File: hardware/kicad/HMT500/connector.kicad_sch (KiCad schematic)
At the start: 10 parts, among them J1 SM08B-GHS-TB, J5 Chassis contact

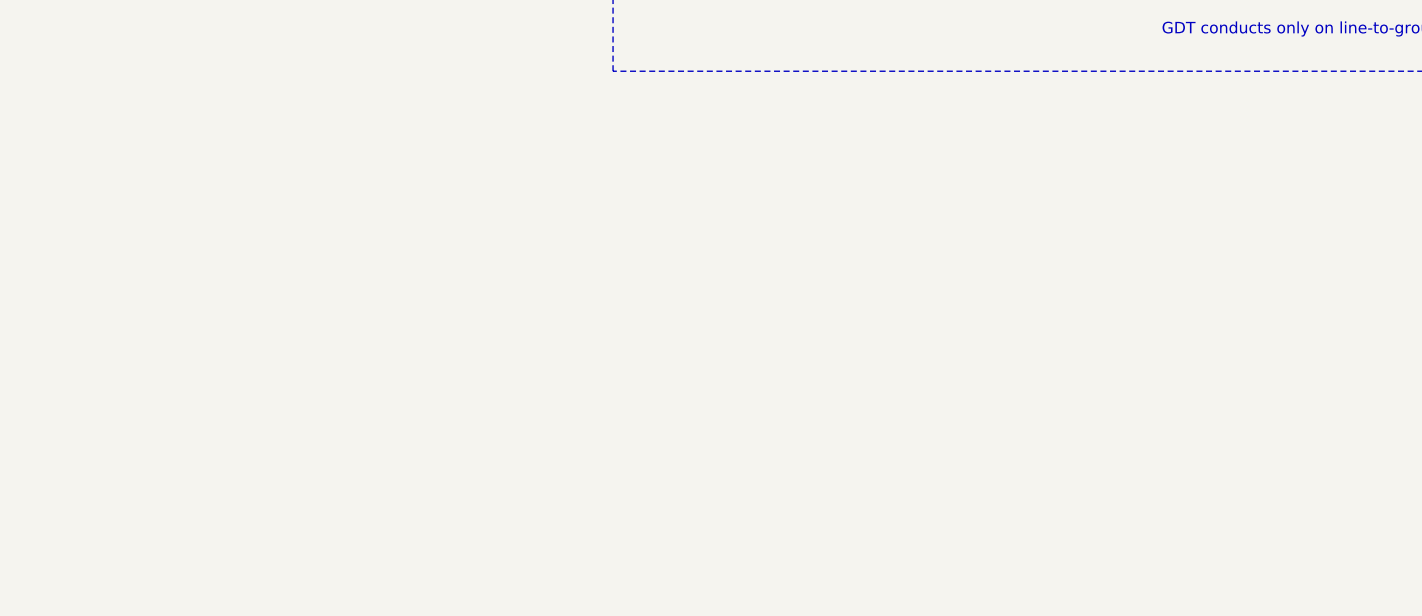
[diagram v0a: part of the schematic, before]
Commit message: Schematic: key-parts table (role, features, specs) on every sheet
- Aligned 4-column table per sheet: reference, part, role, features/specs;
  values still to confirm against datasheets marked with *
- Connector and RS-485 sheets moved to A3 for room
- New checks: text and boxes stay inside the page and out of the title block;
  every character of Hangul text must exist in NanumGothic (minus sign and micro
  sign substituted)

Co-Authored-By: Claude Opus 5.5 <noreply@anthropic.com>
Claude-Session: https://claude.ai/code/session_01JA2o8uJsqp9Vzsg4b665ev
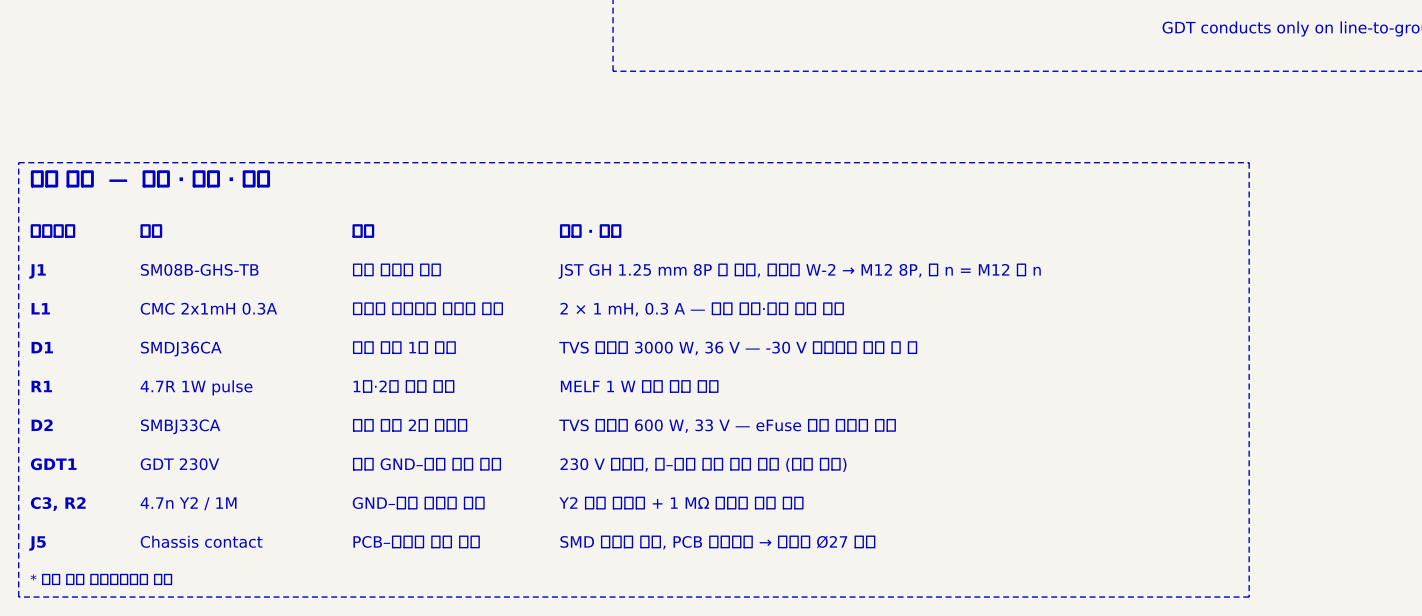
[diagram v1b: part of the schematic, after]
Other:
- note added: "* 표시 값은 데이터시트로 확인"
- note added: "1단·2단 서지 분담"
- note added: "2 × 1 mH, 0.3 A — 전도 방출·전도 내성 대책"
- note added: "230 V 방전관, 선–대지 서지 때만 도통 (평소 절연)"
- note added: "4.7R 1W pulse"
- note added: "4.7n Y2 / 1M"
- note added: "C3, R2"
- note added: "CMC 2x1mH 0.3A"
- note added: "Chassis contact"
- note added: "D1"
- note added: "D2"
- note added: "GDT 230V"
- note added: "GDT1"
- note added: "GND–외함 고주파 결합"
- note added: "J1"
- note added: "J5"
- note added: "JST GH 1.25 mm 8P 옆 삽입, 하네스 W-2 → M12 8P, 핀 n = M12 핀 n"
- note added: "L1"
- note added: "MELF 1 W 펄스 내량 저항"
- note added: "PCB–하우징 접지 접점"
- note added: "R1"
- note added: "SM08B-GHS-TB"
- note added: "SMBJ33CA"
- note added: "SMD 스프링 접점, PCB 가장자리 → 하우징 Ø27 내면"
- note added: "SMDJ36CA"
- note added: "TVS 양방향 3000 W, 36 V — -30 V 오결선에 도통 안 함"
- note added: "TVS 양방향 600 W, 33 V — eFuse 정격 이하로 제한"
- note added: "Y2 안전 콘덴서 + 1 MΩ 정전기 방전 경로"
- note added: "부품"
- note added: "부품번호"
- note added: "역할"
- note added: "입력 서지 1단 흡수"
- note added: "입력 서지 2단 클램프"
- note added: "전원선 공통모드 노이즈 차단"
- note added: "주요 부품 — 역할 · 특징 · 사양"
- note added: "특징 · 사양"
- note added: "현장 커넥터 연결"
- note added: "회로 GND–외함 서지 방전"
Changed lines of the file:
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@@
-(kicad_sch (version 20230121) (generator eeschema) (paper "A4")
+(kicad_sch (version 20230121) (generator eeschema) (paper "A3")
 (title_block (title "HMT500  Connector & input protection") (date "2026-09-29") (rev "0.6") (company "DOTECH Co., Ltd.") (comment 1 "Oil moisture transmitter HMT500 - RS-485 + 2x V/I analog output") (comment 2 "Design notes: docs/hw/circuit-design.md") (comment 3 "VERIFY=YES parts: pin numbers LMR36006/PCAP04/DAC8760/TPS26611; TPS2660 R22"))
 (symbol (lib_id "HMT500:CONN_GH8") (at 45.72 78.74 0) (unit 1) (in_bom yes) (on_board yes) (dnp no) (property "Reference" "J1" (at 38.1 64.77 0) (effects (font (size 1.27 1.27) bold) (justify left))) (property "Value" "SM08B-GHS-TB" (at 38.1 67.056 0) (effects (font (size 1.27 1.27)) (justify left))) (property "Footprint" "Connector_JST:JST_GH_SM08B-GHS-TB_1x08-1MP_P1.25mm_Horizontal" (at 45.72 78.74 0) (effects (font (size 1.27 1.27)) hide)) (property "Datasheet" "~" (at 45.72 78.74 0) (effects (font (size 1.27 1.27)) hide)) (pin "8") (pin "6") (pin "4") (pin "5") (pin "3") (pin "2") (pin "1") (pin "7") (instances (project "HMT500" (path "/1ebb025b-11bd-5f7c-aaab-41e2a750e8b3/d8924d4b-0329-5e79-8dd6-1c12c7722a4b" (reference "J1") (unit 1)))))
@@
 (rectangle (start 78.74 48.26) (end 195.58 93.98) (stroke (width 0.1524) (type dash) (color 72 72 160 1)) (fill (type none)))
 (rectangle (start 86.36 105.41) (end 195.58 142.24) (stroke (width 0.1524) (type dash) (color 72 72 160 1)) (fill (type none)))
+(rectangle (start 20.32 152.4) (end 157.041 200.66) (stroke (width 0.1524) (type dash) (color 72 72 160 1)) (fill (type none)))
 (text "FIELD CONNECTOR" (at 26.67 51.308 0) (effects (font (size 1.6 1.6) bold) (justify left bottom)))
 (text "현장 커넥터" (at 57.696 51.308 0) (effects (font (face "NanumGothic") (size 1.4 1.4)) (justify left bottom)))
@@
 (text "GDT conducts only on line-to-ground surge" (at 147.32 138.43 0) (effects (font (size 1.27 1.27)) (justify left bottom)))
 (text "PCB-housing creepage >= 2 mm" (at 147.32 132.08 0) (effects (font (size 1.27 1.27)) (justify left bottom)))
+(text "부품번호" (at 21.59 161.036 0) (effects (font (face "NanumGothic") (size 1.27 1.27) bold) (justify left bottom)))
+(text "부품" (at 33.7871 161.036 0) (effects (font (face "NanumGothic") (size 1.27 1.27) bold) (justify left bottom)))
+(text "역할" (at 57.3456 161.036 0) (effects (font (face "NanumGothic") (size 1.27 1.27) bold) (justify left bottom)))
+(text "특징 · 사양" (at 80.3961 161.036 0) (effects (font (face "NanumGothic") (size 1.27 1.27) bold) (justify left bottom)))
+(text "J1" (at 21.59 165.354 0) (effects (font (size 1.27 1.27) bold) (justify left bottom)))
+(text "SM08B-GHS-TB" (at 33.7871 165.354 0) (effects (font (size 1.27 1.27)) (justify left bottom)))
+(text "현장 커넥터 연결" (at 57.3456 165.354 0) (effects (font (face "NanumGothic") (size 1.27 1.27)) (justify left bottom)))
+(text "JST GH 1.25 mm 8P 옆 삽입, 하네스 W-2 → M12 8P, 핀 n = M12 핀 n" (at 80.3961 165.354 0) (effects (font (face "NanumGothic") (size 1.27 1.27)) (justify left bottom)))
+(text "L1" (at 21.59 169.672 0) (effects (font (size 1.27 1.27) bold) (justify left bottom)))
+(text "CMC 2x1mH 0.3A" (at 33.7871 169.672 0) (effects (font (size 1.27 1.27)) (justify left bottom)))
+(text "전원선 공통모드 노이즈 차단" (at 57.3456 169.672 0) (effects (font (face "NanumGothic") (size 1.27 1.27)) (justify left bottom)))
+(text "2 × 1 mH, 0.3 A — 전도 방출·전도 내성 대책" (at 80.3961 169.672 0) (effects (font (face "NanumGothic") (size 1.27 1.27)) (justify left bottom)))
+(text "D1" (at 21.59 173.99 0) (effects (font (size 1.27 1.27) bold) (justify left bottom)))
+(text "SMDJ36CA" (at 33.7871 173.99 0) (effects (font (size 1.27 1.27)) (justify left bottom)))
+(text "입력 서지 1단 흡수" (at 57.3456 173.99 0) (effects (font (face "NanumGothic") (size 1.27 1.27)) (justify left bottom)))
+(text "TVS 양방향 3000 W, 36 V — -30 V 오결선에 도통 안 함" (at 80.3961 173.99 0) (effects (font (face "NanumGothic") (size 1.27 1.27)) (justify left bottom)))
+(text "R1" (at 21.59 178.308 0) (effects (font (size 1.27 1.27) bold) (justify left bottom)))
+(text "4.7R 1W pulse" (at 33.7871 178.308 0) (effects (font (size 1.27 1.27)) (justify left bottom)))
+(text "1단·2단 서지 분담" (at 57.3456 178.308 0) (effects (font (face "NanumGothic") (size 1.27 1.27)) (justify left bottom)))
+(text "MELF 1 W 펄스 내량 저항" (at 80.3961 178.308 0) (effects (font (face "NanumGothic") (size 1.27 1.27)) (justify left bottom)))
+(text "D2" (at 21.59 182.626 0) (effects (font (size 1.27 1.27) bold) (justify left bottom)))
+(text "SMBJ33CA" (at 33.7871 182.626 0) (effects (font (size 1.27 1.27)) (justify left bottom)))
+(text "입력 서지 2단 클램프" (at 57.3456 182.626 0) (effects (font (face "NanumGothic") (size 1.27 1.27)) (justify left bottom)))
+(text "TVS 양방향 600 W, 33 V — eFuse 정격 이하로 제한" (at 80.3961 182.626 0) (effects (font (face "NanumGothic") (size 1.27 1.27)) (justify left bottom)))
+(text "GDT1" (at 21.59 186.944 0) (effects (font (size 1.27 1.27) bold) (justify left bottom)))
+(text "GDT 230V" (at 33.7871 186.944 0) (effects (font (size 1.27 1.27)) (justify left bottom)))
+(text "회로 GND–외함 서지 방전" (at 57.3456 186.944 0) (effects (font (face "NanumGothic") (size 1.27 1.27)) (justify left bottom)))
+(text "230 V 방전관, 선–대지 서지 때만 도통 (평소 절연)" (at 80.3961 186.944 0) (effects (font (face "NanumGothic") (size 1.27 1.27)) (justify left bottom)))
+(text "C3, R2" (at 21.59 191.262 0) (effects (font (size 1.27 1.27) bold) (justify left bottom)))
+(text "4.7n Y2 / 1M" (at 33.7871 191.262 0) (effects (font (size 1.27 1.27)) (justify left bottom)))
+(text "GND–외함 고주파 결합" (at 57.3456 191.262 0) (effects (font (face "NanumGothic") (size 1.27 1.27)) (justify left bottom)))
+(text "Y2 안전 콘덴서 + 1 MΩ 정전기 방전 경로" (at 80.3961 191.262 0) (effects (font (face "NanumGothic") (size 1.27 1.27)) (justify left bottom)))
+(text "J5" (at 21.59 195.58 0) (effects (font (size 1.27 1.27) bold) (justify left bottom)))
+(text "Chassis contact" (at 33.7871 195.58 0) (effects (font (size 1.27 1.27)) (justify left bottom)))
+(text "PCB–하우징 접지 접점" (at 57.3456 195.58 0) (effects (font (face "NanumGothic") (size 1.27 1.27)) (justify left bottom)))
+(text "SMD 스프링 접점, PCB 가장자리 → 하우징 Ø27 내면" (at 80.3961 195.58 0) (effects (font (face "NanumGothic") (size 1.27 1.27)) (justify left bottom)))
+(text "주요 부품  —  역할 · 특징 · 사양" (at 21.59 155.448 0) (effects (font (face "NanumGothic") (size 1.6 1.6) bold) (justify left bottom)))
+(text "* 표시 값은 데이터시트로 확인" (at 21.59 199.644 0) (effects (font (face "NanumGothic") (size 1.1 1.1)) (justify left bottom)))
 )
